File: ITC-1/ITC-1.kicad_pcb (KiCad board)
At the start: 2 copper layers, 46 x 46 mm, 23 parts, among them K1 кнопка, K2 кнопка, X1 крепеж, X2 крепеж

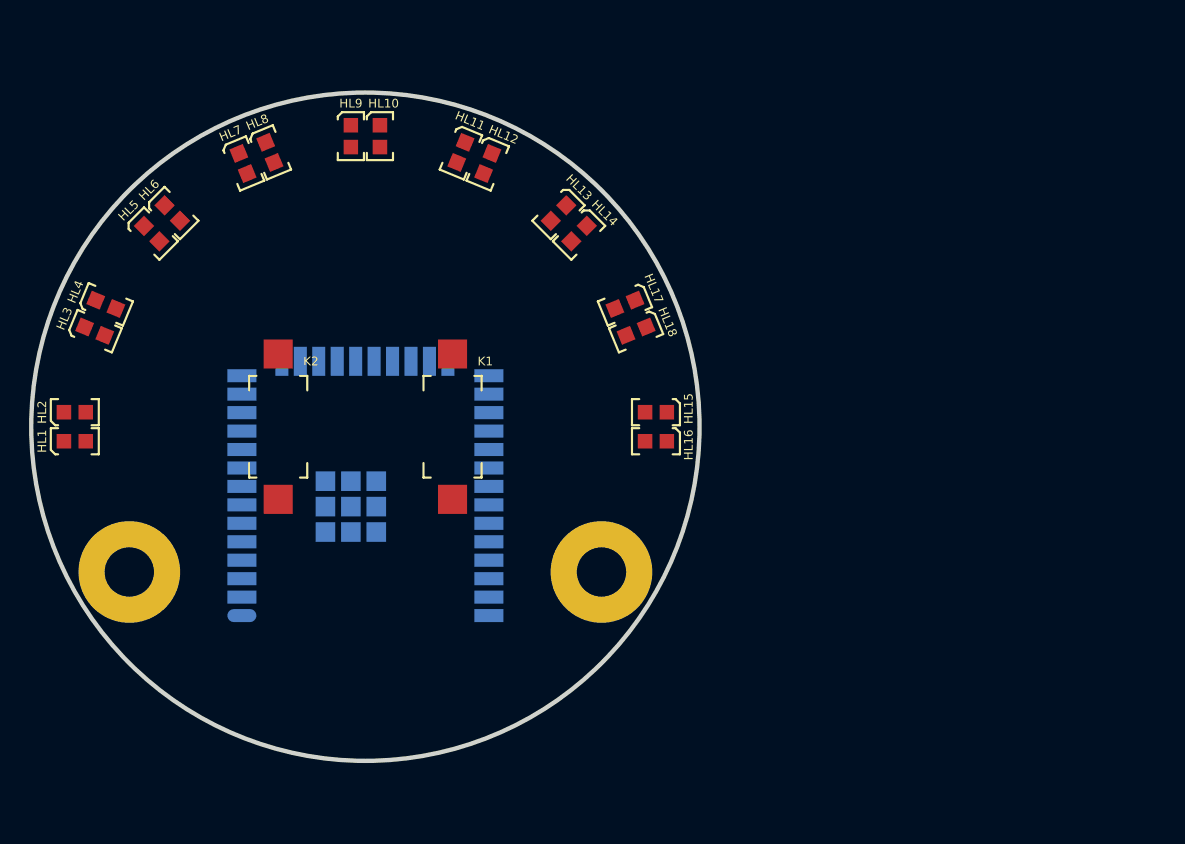
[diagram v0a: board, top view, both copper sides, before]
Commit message: расположено управление светодиодами
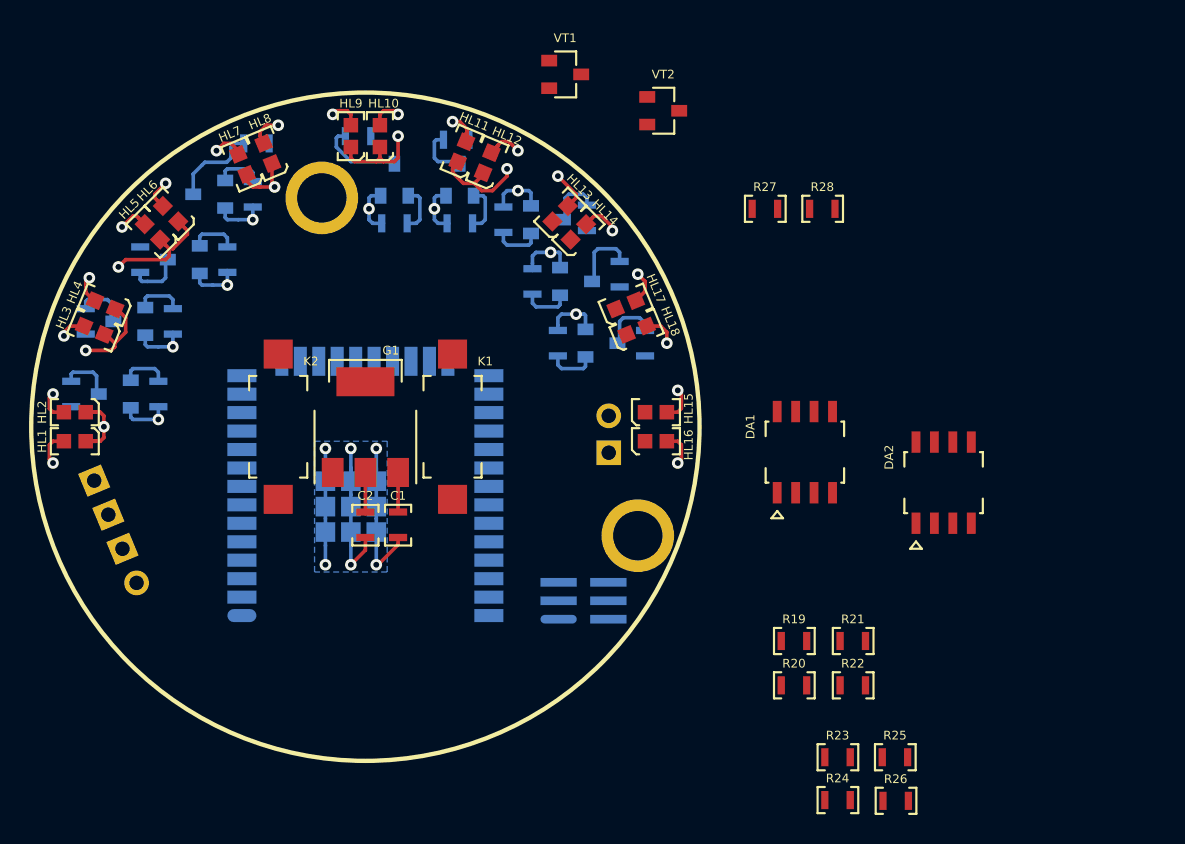
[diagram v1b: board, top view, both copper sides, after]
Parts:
- added C1: Конденсатор_керамический, N_RLC:Конденсатор_SMD_0603_pnp, F.Cu at (102.2, 81.8)
- added C2: Конденсатор_керамический, N_RLC:Конденсатор_SMD_0603_pnp, F.Cu at (100.0, 81.8)
- added DA1: ОУ_LMx58, N_DD:SO-8, F.Cu at (130.2, 76.8)
- added DA2: ОУ_LMx58, N_DD:SO-8, F.Cu at (139.8, 78.8)
- added G1: стабилизатор_нерегулируемый_LM1117S33, N_VD_HL:Транзистор_NPN_SOT223_pnp, F.Cu at (100.0, 75.0)
- added R1: Резистор_0,065Вт, N_RLC:Резистор_SMD_0603_0,065_Вт_pnp, B.Cu at (85.8, 72.8)
- added R10: Резистор_0,065Вт, N_RLC:Резистор_SMD_0603_0,065_Вт_pnp, B.Cu at (84.5, 63.5)
- added R11: Резистор_0,065Вт, N_RLC:Резистор_SMD_0603_0,065_Вт_pnp, B.Cu at (92.5, 55.5)
- added R12: Резистор_0,065Вт, N_RLC:Резистор_SMD_0603_0,065_Вт_pnp, B.Cu at (99.5, 55.0)
- added R13: Резистор_0,065Вт, N_RLC:Резистор_SMD_0603_0,065_Вт_pnp, B.Cu at (106.2, 55.2)
- added R14: Резистор_0,065Вт, N_RLC:Резистор_SMD_0603_0,065_Вт_pnp, B.Cu at (115.2, 60.6)
- added R15: Резистор_0,065Вт, N_RLC:Резистор_SMD_0603_0,065_Вт_pnp, B.Cu at (111.5, 65.0)
- added R16: Резистор_0,065Вт, N_RLC:Резистор_SMD_0603_0,065_Вт_pnp, B.Cu at (113.2, 69.2)
- added R17: Резистор_0,065Вт, N_RLC:Резистор_SMD_0603_0,065_Вт_pnp, B.Cu at (117.5, 64.5)
- added R18: Резистор_0,065Вт, N_RLC:Резистор_SMD_0603_0,065_Вт_pnp, B.Cu at (119.2, 69.2)
- added R19: Резистор_0,065Вт, N_RLC:Резистор_SMD_0603_0,065_Вт_pnp, F.Cu at (129.5, 89.8)
- added R2: Резистор_0,065Вт, N_RLC:Резистор_SMD_0603_0,065_Вт_pnp, B.Cu at (86.8, 67.8)
- added R20: Резистор_0,065Вт, N_RLC:Резистор_SMD_0603_0,065_Вт_pnp, F.Cu at (129.5, 92.8)
- added R21: Резистор_0,065Вт, N_RLC:Резистор_SMD_0603_0,065_Вт_pnp, F.Cu at (133.6, 89.8)
- added R22: Резистор_0,065Вт, N_RLC:Резистор_SMD_0603_0,065_Вт_pnp, F.Cu at (133.6, 92.8)
- added R23: Резистор_0,065Вт, N_RLC:Резистор_SMD_0603_0,065_Вт_pnp, F.Cu at (132.5, 97.8)
- added R24: Резистор_0,065Вт, N_RLC:Резистор_SMD_0603_0,065_Вт_pnp, F.Cu at (132.5, 100.7)
- added R25: Резистор_0,065Вт, N_RLC:Резистор_SMD_0603_0,065_Вт_pnp, F.Cu at (136.4, 97.8)
- added R26: Резистор_0,065Вт, N_RLC:Резистор_SMD_0603_0,065_Вт_pnp, F.Cu at (136.5, 100.8)
- added R27: Резистор_0,065Вт, N_RLC:Резистор_SMD_0603_0,065_Вт_pnp, F.Cu at (127.5, 60.0)
- added R28: Резистор_0,065Вт, N_RLC:Резистор_SMD_0603_0,065_Вт_pnp, F.Cu at (131.4, 60.0)
- added R3: Резистор_0,065Вт, N_RLC:Резистор_SMD_0603_0,065_Вт_pnp, B.Cu at (79.8, 72.8)
- added R4: Резистор_0,065Вт, N_RLC:Резистор_SMD_0603_0,065_Вт_pnp, B.Cu at (80.8, 67.8)
- added R5: Резистор_0,065Вт, N_RLC:Резистор_SMD_0603_0,065_Вт_pnp, B.Cu at (90.5, 63.5)
- added R6: Резистор_0,065Вт, N_RLC:Резистор_SMD_0603_0,065_Вт_pnp, B.Cu at (92.2, 59.0)
- added R7: Резистор_0,065Вт, N_RLC:Резистор_SMD_0603_0,065_Вт_pnp, B.Cu at (102.0, 61.0)
- added R8: Резистор_0,065Вт, N_RLC:Резистор_SMD_0603_0,065_Вт_pnp, B.Cu at (106.5, 61.0)
- added R9: Резистор_0,065Вт, N_RLC:Резистор_SMD_0603_0,065_Вт_pnp, B.Cu at (109.5, 60.8)
- added VT1: Транзистор_полевой_P-канал(IRLML2246TRPBF), N_VD_HL:Транзистор_IRLML6344TR_SOT-23, F.Cu at (113.8, 50.8)
- added VT10: Транзистор_полевой_N-IRLML6344TR, N_VD_HL:Транзистор_IRLML6344TR_SOT-23, B.Cu at (114.5, 65.0)
- added VT11: Транзистор_полевой_N-IRLML6344TR, N_VD_HL:Транзистор_IRLML6344TR_SOT-23, B.Cu at (116.2, 69.2)
- added VT2: Транзистор_полевой_P-канал(IRLML2246TRPBF), N_VD_HL:Транзистор_IRLML6344TR_SOT-23, F.Cu at (120.5, 53.2)
- added VT3: Транзистор_полевой_N-IRLML6344TR, N_VD_HL:Транзистор_IRLML6344TR_SOT-23, B.Cu at (82.8, 72.8)
- added VT4: Транзистор_полевой_N-IRLML6344TR, N_VD_HL:Транзистор_IRLML6344TR_SOT-23, B.Cu at (83.8, 67.8)
- added VT5: Транзистор_полевой_N-IRLML6344TR, N_VD_HL:Транзистор_IRLML6344TR_SOT-23, B.Cu at (87.5, 63.5)
- added VT6: Транзистор_полевой_N-IRLML6344TR, N_VD_HL:Транзистор_IRLML6344TR_SOT-23, B.Cu at (89.2, 59.0)
- added VT7: Транзистор_полевой_N-IRLML6344TR, N_VD_HL:Транзистор_IRLML6344TR_SOT-23, B.Cu at (102.0, 58.0)
- added VT8: Транзистор_полевой_N-IRLML6344TR, N_VD_HL:Транзистор_IRLML6344TR_SOT-23, B.Cu at (106.5, 58.0)
- added VT9: Транзистор_полевой_N-IRLML6344TR, N_VD_HL:Транзистор_IRLML6344TR_SOT-23, B.Cu at (112.5, 60.8)
- added XP1: Вилка_PLD6_ПРОГ_STM, N_X:Вилка_PLLD6_угловая_вертикальная, B.Cu at (114.2, 88.2)
- added XP2: Клеммник_х2, N_X:Вилка_XH2.54-2_вертикальная, B.Cu at (116.8, 74.2)
- added XP3: Клеммник_х4, N_X:Вилка_XH2.54-4_вертикальная, B.Cu at (84.2, 85.8)
- moved X1 29.0 mm to (97.0, 59.2)
- moved X2 3.54 mm to (118.8, 82.5)
- moved HL11 1.56 mm to (106.9, 55.4), turned to 247.5 degrees
- moved HL18 1.56 mm to (119.4, 68.1), turned to 202.5 degrees
- moved HL3 1.56 mm to (80.6, 68.1), turned to 337.5 degrees
- moved HL13 1.55 mm to (113.9, 59.8), turned to 225 degrees
- moved HL14 1.55 mm to (115.2, 61.1), turned to 225 degrees
- moved HL5 1.55 mm to (84.8, 61.1), turned to 315 degrees
- moved HL6 1.55 mm to (86.1, 59.8), turned to 315 degrees
- moved HL12 1.54 mm to (108.7, 56.1), turned to 247.5 degrees
- moved HL17 1.54 mm to (118.6, 66.3), turned to 202.5 degrees
- moved HL4 1.54 mm to (81.4, 66.3), turned to 337.5 degrees
- moved HL1 1.50 mm to (79.2, 76.0), turned to 0 degrees
- moved HL10 1.50 mm to (101.0, 54.2), turned to 270 degrees
- moved HL15 1.50 mm to (120.8, 74.0), turned to 180 degrees
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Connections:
- A1 pad 1: Net-(A1-Pad1) -> /GND
- A1 pad 10: Net-(A1-Pad10) -> /LED_5
- A1 pad 11: Net-(A1-Pad11) -> /LED_6
- A1 pad 12: Net-(A1-Pad12) -> /LED_7
- A1 pad 13: Net-(A1-Pad13) -> /LED_8
- A1 pad 15: Net-(A1-Pad15) -> /GND
- A1 pad 16: Net-(A1-Pad16) -> /LED_9
- A1 pad 2: Net-(A1-Pad2) -> /3V3
- A1 pad 23: Net-(A1-Pad23) -> /LED_GREEN
- A1 pad 24: Net-(A1-Pad24) -> /LED_RED
- A1 pad 25: Net-(A1-Pad25) -> /BOOT_SEL
- A1 pad 26: Net-(A1-Pad26) -> /BUTT_1
- A1 pad 27: Net-(A1-Pad27) -> /BUTT_2
- A1 pad 3: Net-(A1-Pad3) -> /EN_RESET
- A1 pad 34: Net-(A1-Pad34) -> /BOOT_UART_RX
- A1 pad 35: Net-(A1-Pad35) -> /BOOT_UART_TX
- A1 pad 38: Net-(A1-Pad38) -> /GND
- A1 pad 39: Net-(A1-Pad39) -> /GND
- A1 pad 6: Net-(A1-Pad6) -> /LED_1
- A1 pad 7: Net-(A1-Pad7) -> /LED_2
- A1 pad 8: Net-(A1-Pad8) -> /LED_3
- A1 pad 9: Net-(A1-Pad9) -> /LED_4
- HL1 pad 1: Net-(HL1-Pad1) -> /3V3-RED
- HL10 pad 1: Net-(HL10-Pad1) -> /3V3-GREEN
- HL11 pad 1: Net-(HL11-Pad1) -> /3V3-RED
- HL12 pad 1: Net-(HL12-Pad1) -> /3V3-GREEN
- HL12 pad 2: Net-(HL12-Pad2) -> Net-(HL11-Pad2)
- HL13 pad 1: Net-(HL13-Pad1) -> /3V3-RED
- HL14 pad 1: Net-(HL14-Pad1) -> /3V3-GREEN
- HL14 pad 2: Net-(HL14-Pad2) -> Net-(HL13-Pad2)
- HL15 pad 1: Net-(HL15-Pad1) -> /3V3-RED
- HL16 pad 1: Net-(HL16-Pad1) -> /3V3-GREEN
- HL16 pad 2: Net-(HL16-Pad2) -> Net-(HL15-Pad2)
- HL17 pad 1: Net-(HL17-Pad1) -> /3V3-RED
- HL18 pad 1: Net-(HL18-Pad1) -> /3V3-GREEN
- HL18 pad 2: Net-(HL18-Pad2) -> Net-(HL17-Pad2)
- HL2 pad 1: Net-(HL2-Pad1) -> /3V3-GREEN
- HL2 pad 2: Net-(HL2-Pad2) -> Net-(HL1-Pad2)
- HL3 pad 1: Net-(HL3-Pad1) -> /3V3-RED
- HL4 pad 1: Net-(HL4-Pad1) -> /3V3-GREEN
- HL4 pad 2: Net-(HL4-Pad2) -> Net-(HL3-Pad2)
- HL5 pad 1: Net-(HL5-Pad1) -> /3V3-RED
- HL6 pad 1: Net-(HL6-Pad1) -> /3V3-GREEN
- HL6 pad 2: Net-(HL6-Pad2) -> Net-(HL5-Pad2)
- HL7 pad 1: Net-(HL7-Pad1) -> /3V3-RED
- HL8 pad 1: Net-(HL8-Pad1) -> /3V3-GREEN
- HL8 pad 2: Net-(HL8-Pad2) -> Net-(HL7-Pad2)
- HL9 pad 1: Net-(HL9-Pad1) -> /3V3-RED
- HL9 pad 2: Net-(HL9-Pad2) -> Net-(HL10-Pad2)
- K1 pad 2: Net-(K1-Pad2) -> /GND
- K2 pad 2: Net-(K2-Pad2) -> /GND
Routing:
- net /3V3-RED: track 0.00 -> 94.8 mm, vias 0 -> 9
- net /3V3-GREEN: track 0.00 -> 93.3 mm, vias 0 -> 9
- net /GND: track 0.00 -> 63.7 mm, vias 0 -> 15
- net Net-(HL5-Pad2): track 0.00 -> 8.00 mm, vias 0 -> 1
- net Net-(HL10-Pad2): track 0.00 -> 7.16 mm, vias 0 -> 1
- net Net-(HL11-Pad2): track 0.00 -> 6.76 mm, vias 0 -> 1
- net Net-(R11-Pad2): track 0.00 -> 6.31 mm
- net Net-(HL3-Pad2): track 0.00 -> 6.10 mm, vias 0 -> 1
- net Net-(R12-Pad2): track 0.00 -> 5.72 mm
- net Net-(HL1-Pad2): track 0.00 -> 5.71 mm, vias 0 -> 1
- net Net-(R17-Pad2): track 0.00 -> 4.58 mm
- net Net-(HL7-Pad2): track 0.00 -> 4.23 mm, vias 0 -> 1
- net Net-(R18-Pad2): track 0.00 -> 4.01 mm
- net Net-(R14-Pad2): track 0.00 -> 3.71 mm
- net Net-(R4-Pad2): track 0.00 -> 3.66 mm
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- added copper zone on B.Cu, net /GND
- added copper zone on In1.Cu, net /GND
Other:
- board outline removed
- copper layers 2 -> 4

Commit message: заменены разъемы, исключены ОУ, определена распиновка и упр. транзистор
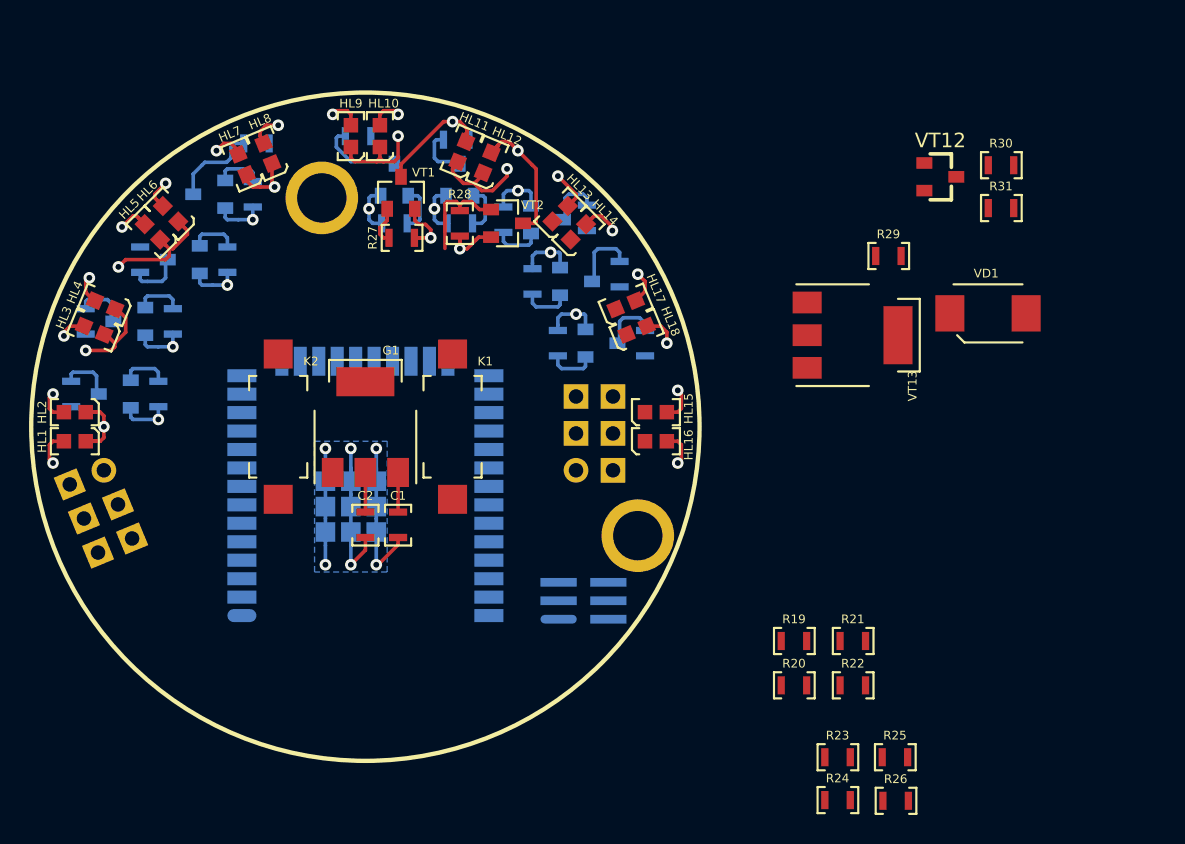
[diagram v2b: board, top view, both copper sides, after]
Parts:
- removed DA1, DA2: ОУ_LMx58, N_DD:SO-8
- removed XP2: Клеммник_х2, N_X:Вилка_XH2.54-2_вертикальная
- removed XP3: Клеммник_х4, N_X:Вилка_XH2.54-4_вертикальная
- added R29: Резистор_0,065Вт, N_RLC:Резистор_SMD_0603_0,065_Вт_pnp, F.Cu at (136.0, 63.2)
- added R30: Резистор_0,065Вт, N_RLC:Резистор_SMD_0603_0,065_Вт_pnp, F.Cu at (143.8, 57.0)
- added R31: Резистор_0,065Вт, N_RLC:Резистор_SMD_0603_0,065_Вт_pnp, F.Cu at (143.8, 60.0)
- added VD1: Диод_шоттки, N_VD_HL:Диод_SMB_pnp, F.Cu at (142.9, 67.2)
- added VT12: Транзистор_полевой_N-IRLML6344TR, N_VD_HL:Транзистор_IRLML6344TR_SOT-23, F.Cu at (139.6, 57.8)
- added VT13: Транзистор_NPN_1Б-2(4)К-3Э_0, N_VD_HL:Транзистор_NPN_SOT223_pnp, F.Cu at (133.6, 68.7)
- added XP4: Вилка_PLS6, N_X:Вилка_PLD6_вертикальная, B.Cu at (114.5, 78.0)
- added XP5: Вилка_PLS6, N_X:Вилка_PLD6_вертикальная, B.Cu at (82.0, 78.0)
- moved R27 25.1 mm to (102.5, 62.0)
- moved R28 25.0 mm to (106.5, 61.0), turned to 270 degrees
- moved VT1 13.9 mm to (102.5, 58.9), turned to 90 degrees
- moved VT2 13.3 mm to (109.8, 61.0)
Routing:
- net /3V3: track 2.85 -> 11.0 mm, vias 0 -> 2
- net /LED_GREEN: track 0.00 -> 7.00 mm
- net /3V3-GREEN: track 93.3 -> 99.6 mm
- net /3V3-RED: track 94.8 -> 100.4 mm
- net /LED_RED: track 0.00 -> 2.56 mm
- added copper zone on In2.Cu, net /3V3

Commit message: определено подключение аналоговых входов
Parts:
- added G2: ИОП_LM4040BIM3-2.5_NOPB, MOTOR_VD_VT_HL:Корпус_КТ-46, F.Cu at (138.8, 86.5)
- added R32: Резистор_0,065Вт, N_RLC:Резистор_SMD_0603_0,065_Вт_pnp, F.Cu at (143.0, 85.7)
- added R33: Резистор_0,065Вт, N_RLC:Резистор_SMD_0603_0,065_Вт_pnp, F.Cu at (145.0, 73.0)
- added R34: Резистор_0,065Вт, N_RLC:Резистор_SMD_0603_0,065_Вт_pnp, F.Cu at (145.0, 76.0)
- added R35: Резистор_0,065Вт, N_RLC:Резистор_SMD_0603_0,065_Вт_pnp, F.Cu at (148.9, 73.0)
- added R36: Резистор_0,065Вт, N_RLC:Резистор_SMD_0603_0,065_Вт_pnp, F.Cu at (145.0, 78.9)
- added R37: Резистор_0,065Вт, N_RLC:Резистор_SMD_0603_0,065_Вт_pnp, F.Cu at (148.9, 76.0)
- added R38: Резистор_0,065Вт, N_RLC:Резистор_SMD_0603_0,065_Вт_pnp, F.Cu at (152.9, 73.0)
- added R39: Резистор_0,065Вт, N_RLC:Резистор_SMD_0603_0,065_Вт_pnp, F.Cu at (148.9, 78.9)
- added R40: Резистор_0,065Вт, N_RLC:Резистор_SMD_0603_0,065_Вт_pnp, F.Cu at (152.9, 76.0)
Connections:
- A1 pad 10: /LED_5 -> /LED_2
- A1 pad 11: /LED_6 -> /LED_3
- A1 pad 12: /LED_7 -> /LED_4
- A1 pad 13: /LED_8 -> /LED_5
- A1 pad 28: Net-(A1-Pad28) -> /LED_8
- A1 pad 29: Net-(A1-Pad29) -> /LED_7
- A1 pad 30: Net-(A1-Pad30) -> /LED_6
- A1 pad 36: Net-(A1-Pad36) -> /LED-DRIVE
- A1 pad 37: Net-(A1-Pad37) -> /MOTOR-DRIVE
- A1 pad 4: Net-(A1-Pad4) -> /ADC1-CH0
- A1 pad 5: Net-(A1-Pad5) -> /ADC1-CH3
- A1 pad 6: /LED_1 -> /ADC1-CH6
- A1 pad 7: /LED_2 -> /ADC1-CH7
- A1 pad 8: /LED_3 -> /ADC1-CH4
- A1 pad 9: /LED_4 -> /LED_1

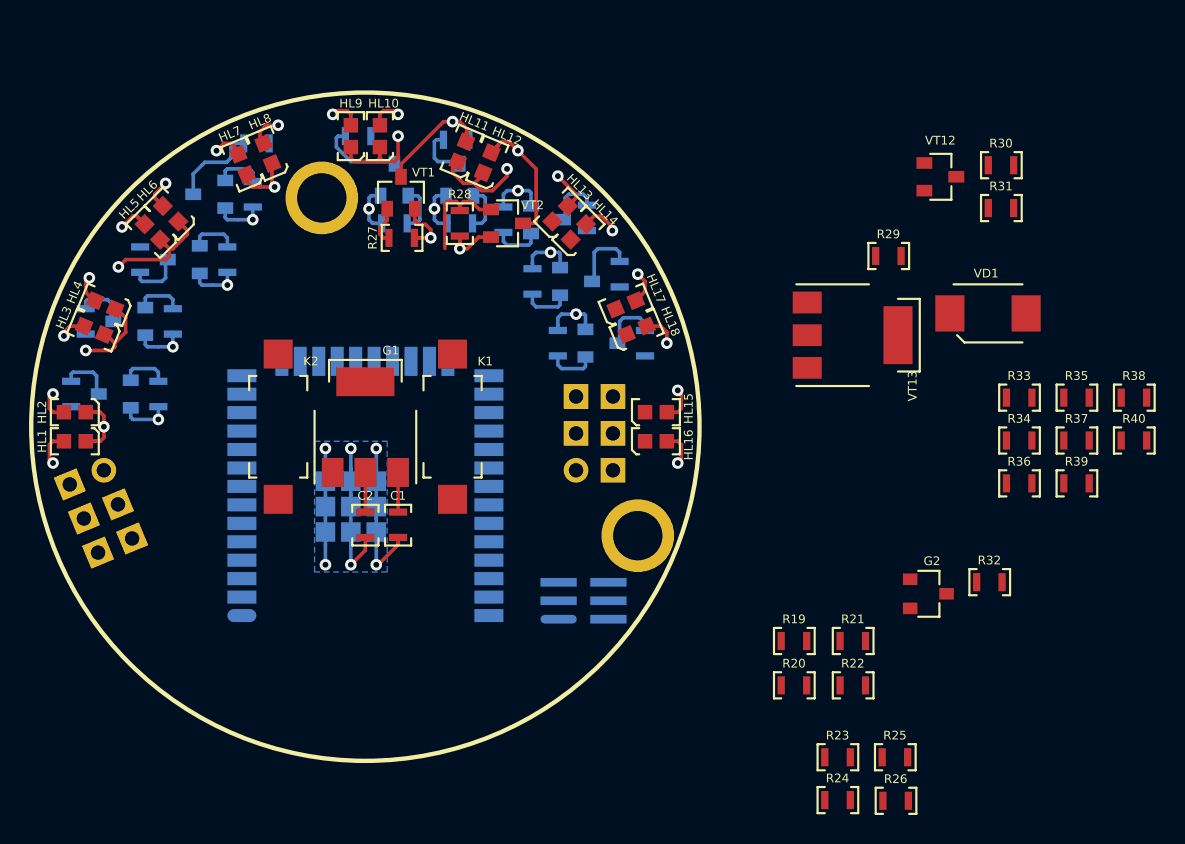
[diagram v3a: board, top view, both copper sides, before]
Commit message: упрощена схема подтяжек, раскинут разъем программирования
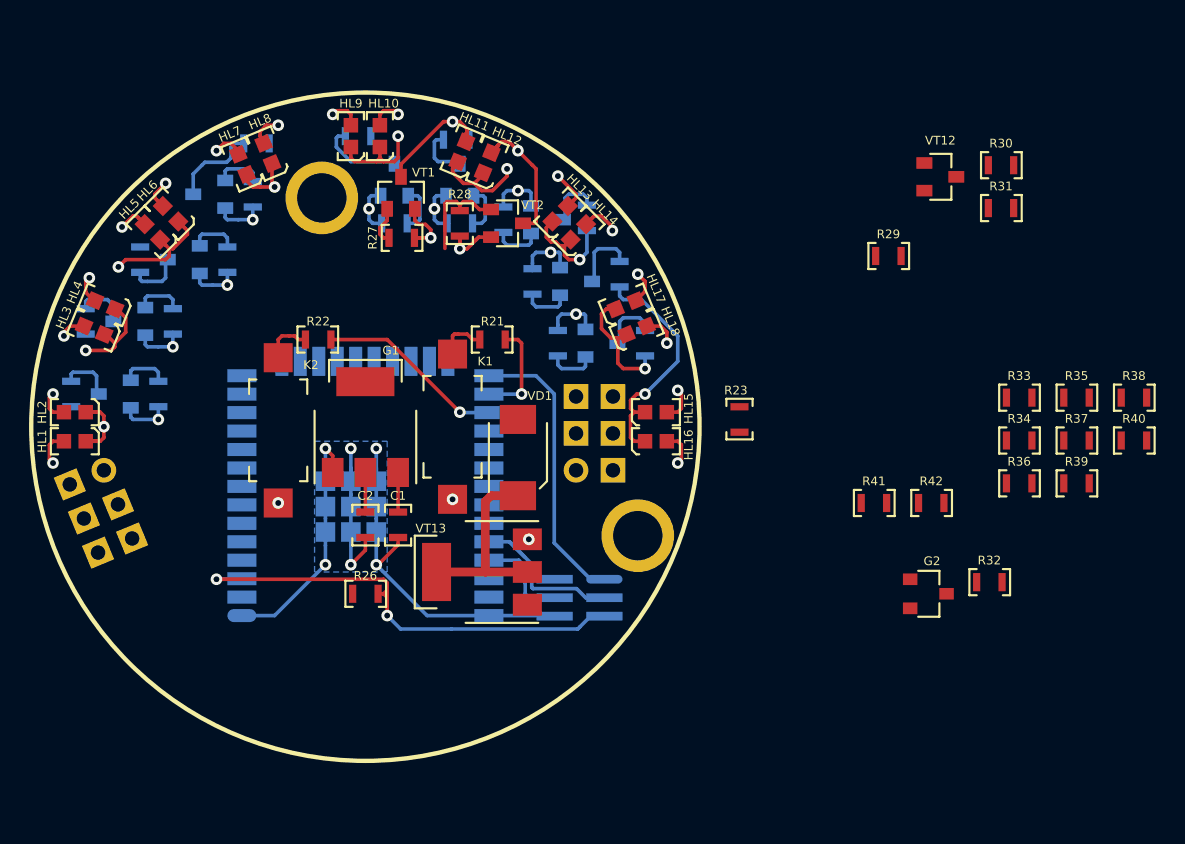
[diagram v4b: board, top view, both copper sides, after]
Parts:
- removed R19, R20, R24, R25: Резистор_0,065Вт, N_RLC:Резистор_SMD_0603_0,065_Вт_pnp
- added R41: Резистор_0,065Вт, N_RLC:Резистор_SMD_0603_0,065_Вт_pnp, F.Cu at (135.0, 80.2)
- added R42: Резистор_0,065Вт, N_RLC:Резистор_SMD_0603_0,065_Вт_pnp, F.Cu at (138.9, 80.2)
- moved R22 43.8 mm to (96.8, 69.0), turned to 180 degrees
- moved R26 39.2 mm to (100.0, 86.5)
- moved VD1 33.8 mm to (110.5, 77.1), turned to 90 degrees
- moved R21 32.3 mm to (108.8, 69.0), turned to 180 degrees
- moved VT13 30.3 mm to (108.0, 85.0), turned to 180 degrees
- moved R23 24.2 mm to (125.8, 74.5), turned to 90 degrees
- moved XP1 3.02 mm to (115.5, 85.5), turned to 270 degrees
- moved K2 0.25 mm to (94.0, 70.2)
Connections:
- A1 pad 33: Net-(A1-Pad33) -> /CHARGE-SENS
- G2 pad 1: /U-REF -> /ADC1-CH4
- R32 pad 2: /U-REF -> /ADC1-CH4
- XP1 pad 1: Net-(R24-Pad2) -> /BOOT_SEL
- XP1 pad 5: Net-(R25-Pad2) -> /EN_RESET
- XP4 pad 2: /CHARGE-SENS -> Net-(R41-Pad2)
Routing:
- net /EN_RESET: track 0.00 -> 31.7 mm, vias 0 -> 2
- net /GND: track 63.7 -> 86.9 mm, vias 15 -> 18
- net /BOOT_SEL: track 0.00 -> 18.8 mm
- net Net-(HL15-Pad2): track 0.00 -> 16.5 mm, vias 0 -> 1
- net /MOTOR-GND: track 0.00 -> 13.5 mm
- net /BUTT_2: track 0.00 -> 13.0 mm, vias 0 -> 1
- net /BOOT_UART_RX: track 0.00 -> 11.0 mm
- net Net-(HL17-Pad2): track 0.00 -> 8.87 mm, vias 0 -> 1
- net /BOOT_UART_TX: track 0.00 -> 7.64 mm
- net Net-(HL13-Pad2): track 0.00 -> 7.39 mm, vias 0 -> 1
- net /BUTT_1: track 0.00 -> 6.98 mm, vias 0 -> 1
- net Net-(K2-Pad1): track 0.00 -> 3.33 mm
- net Net-(K1-Pad1): track 0.00 -> 3.33 mm
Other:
- net class PWR added: clearance 0.2, trace_width 0.6, via_dia 0.8, via_drill 0.4
